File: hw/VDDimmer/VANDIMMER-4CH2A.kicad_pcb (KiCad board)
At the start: 4 copper layers, 100 x 84 mm, 98 parts, among them J1 USB-C 16P, J10 A2 V+SEL VIN/5V, J11 BTN1, J12 BTN2, J13 EXP 3V3/GND/SDA/SCL/EN/IO0, J14 UART1 3V3/GND/TX/RX, J2 VIN 12V, J3 CH1 LED-/V+, J4 CH2 LED-/V+, J5 CH3 LED-/V+, J6 CH4 LED-/V+, J7 ADDR1 V+/D/CLK/GND, J8 ADDR2 V+/D/CLK/GND, J9 A1 V+SEL VIN/5V, Q1 20N06, Q2 20N06, Q3 20N06, Q4 20N06, Q5 SUD50P06-15, U1 ESP32-S3-WROOM-1-N16R8, U2 AP63301WU-7, U3 BL1117-33CX, U4 74HCT125, U5 74HCT125

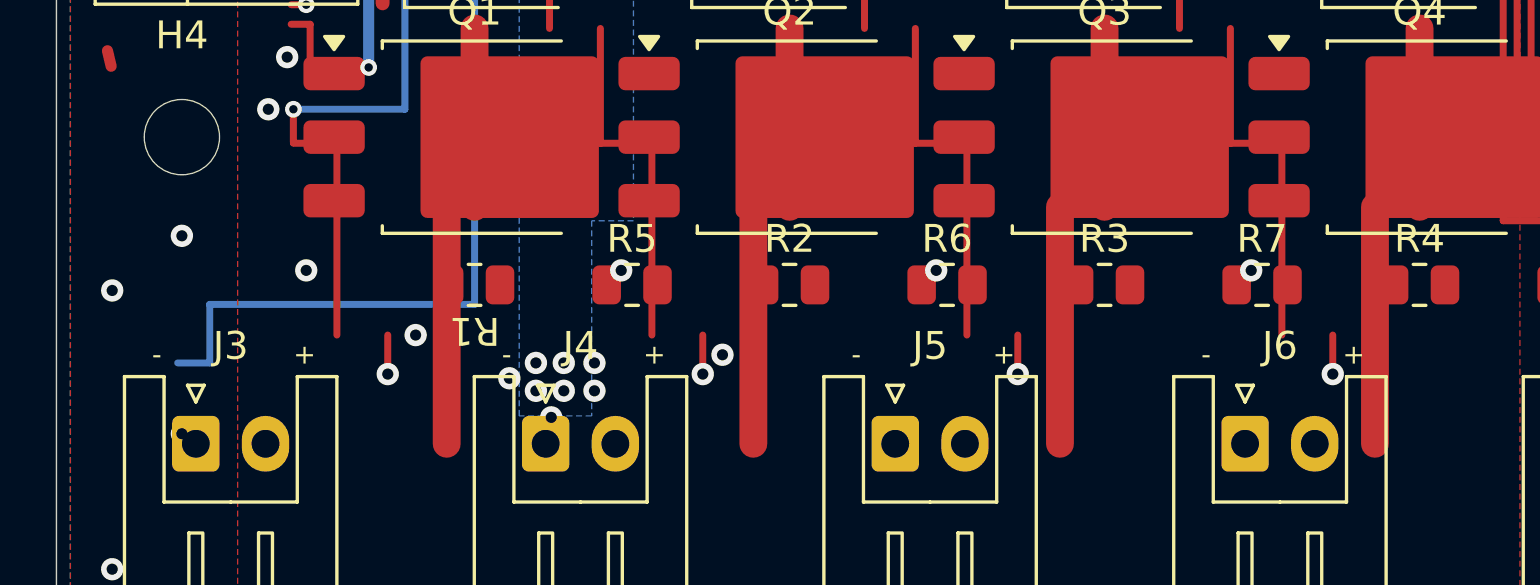
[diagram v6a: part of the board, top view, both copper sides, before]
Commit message: Mark J3-J6 terminals - and +, never GND
Eight F.SilkS marks at 0.8 mm, y 125.91, sitting in the band between the gate
resistors and the connector outlines - the only silk that stays readable once
a connector body is fitted, since the plug approaches from off the board edge.

Verified against NETS, not pin numbers: each - resolves to a DRAINn pad and
each + to VIN_PROT. That is the check that matters, because Rev A carries the
opposite polarity and grounding its pin 1 shorts the supply.

Spec section 6 is explicit that pin 1 must never be marked GND: it is a
switched MOSFET drain, open when the channel is off and floating to ~7 V on an
open terminal from flyback-diode and FET leakage alone.

R1 is rotated 180 -> 0. It was the only one of R1-R8 at 180, which rendered its
reference designator below the part instead of above and put it on top of J4's
- mark. Rotating it matches the rest of the row and clears the overlap; a
220R gate resistor is symmetric so rotation is cosmetic.

Gates: text_height violations 8 -> 0 (the earlier pass used 0.7 mm against the
project's 0.8 mm minimum); zero silk violations involving any polarity mark;
fpspace.py --courtyards still 0 overlaps.

Co-Authored-By: Claude Opus 5 (1M context) <noreply@anthropic.com>
Claude-Session: https://claude.ai/code/session_01YZHVU8aymL4RkLeCfwomwj
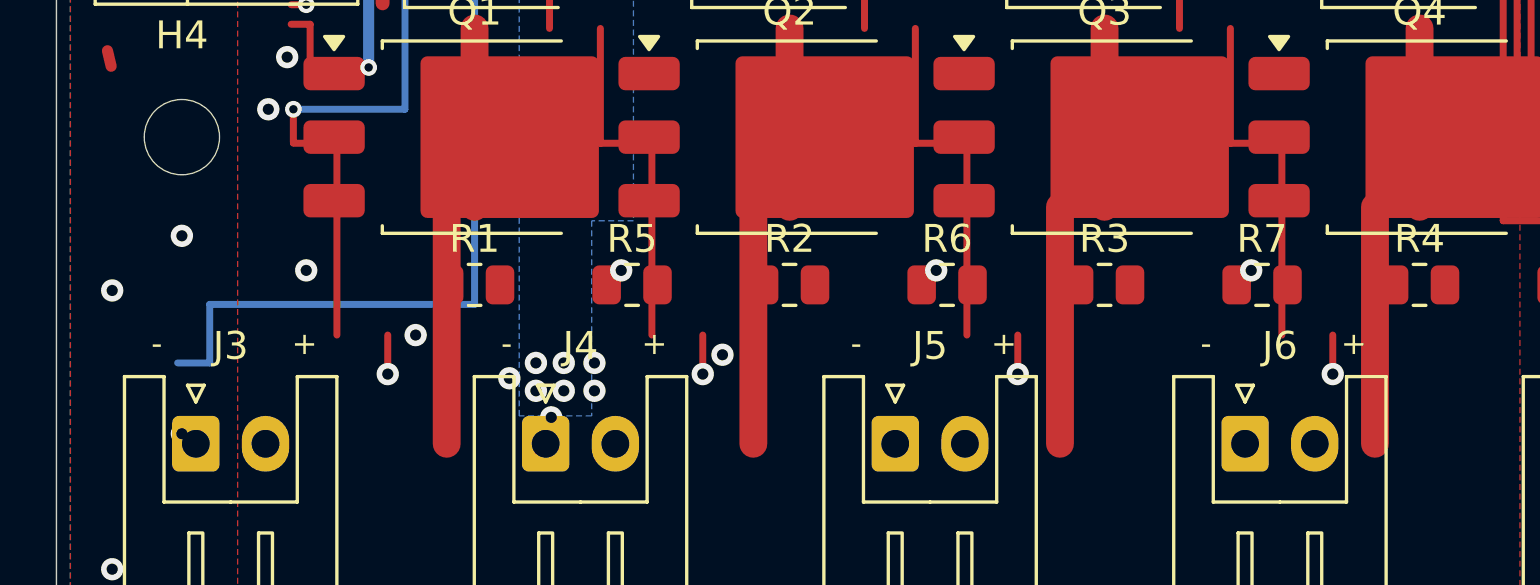
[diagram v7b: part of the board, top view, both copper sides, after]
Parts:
- turned R1 to 0 degrees
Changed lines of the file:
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@@
 	(footprint "Resistor_SMD:R_0805_2012Metric"
 		(layer "F.Cu")
-		(at 115 123.8 180)
+		(at 115 123.8)
 		(descr "Resistor SMD 0805 (2012 Metric), square (rectangular) end terminal, IPC-7351 nominal, (Body size source: IPC-SM-782 page 72, https://www.pcb-3d.com/wordpress/wp-content/uploads/ipc-sm-782a_amendment_1_and_2.pdf)")
 		(tags "resistor")
 		(property "Reference" "R1"
-			(at 0 -1.649999 180)
+			(at 0 -1.649999 0)
 			(unlocked yes)
 			(layer "F.SilkS")
@@
 		)
 		(property "Value" "220R"
-			(at 0 1.65 180)
+			(at 0 1.65 0)
 			(unlocked yes)
 			(layer "F.SilkS")
@@
 		)
 		(property "Datasheet" ""
-			(at 0 0 180)
+			(at 0 0 0)
 			(layer "F.Fab")
 			(hide yes)
@@
 		)
 		(property "Description" ""
-			(at 0 0 180)
+			(at 0 0 0)
 			(layer "F.Fab")
 			(hide yes)
@@
 		)
 		(property "KiLib_Generator" "SMD_2terminal_chip_molded"
-			(at 0 0 180)
+			(at 0 0 0)
 			(layer "F.SilkS")
 			(hide yes)
@@
 		)
 		(property "LCSC" "C17557"
-			(at 0 0 180)
+			(at 0 0 0)
 			(unlocked yes)
 			(layer "F.Fab")
@@
 		)
 		(property "MPN" "0805W8F2200T5E"
-			(at 0 0 180)
+			(at 0 0 0)
 			(unlocked yes)
 			(layer "F.Fab")
@@
 		)
 		(property "Manufacturer" "UNI-ROYAL"
-			(at 0 0 180)
+			(at 0 0 0)
 			(unlocked yes)
 			(layer "F.Fab")
@@
 		(duplicate_pad_numbers_are_jumpers no)
 		(fp_line
-			(start -0.227064 0.735)
-			(end 0.227064 0.735)
+			(start -0.227064 -0.735)
+			(end 0.227064 -0.735)
 			(stroke
 				(width 0.12)
@@
 		)
 		(fp_line
-			(start -0.227064 -0.735)
-			(end 0.227064 -0.735)
+			(start -0.227064 0.735)
+			(end 0.227064 0.735)
 			(stroke
 				(width 0.12)
@@
 		)
 		(fp_text user "${REFERENCE}"
-			(at 0 0 180)
+			(at 0 0 0)
 			(unlocked yes)
 			(layer "F.Fab")
@@
 		)
 		(pad "1" smd roundrect
-			(at -0.9125 0 180)
+			(at -0.9125 0)
 			(size 1.025 1.4)
 			(layers "F.Cu" "F.Mask" "F.Paste")
@@
 		)
 		(pad "2" smd roundrect
-			(at 0.9125 0 180)
+			(at 0.9125 0)
 			(size 1.025 1.4)
 			(layers "F.Cu" "F.Mask" "F.Paste")
@@
 	)
 	(gr_text "-"
-		(at 103.6 126.3 0)
+		(at 103.6 125.91 0)
 		(layer "F.SilkS")
 		(effects
 			(font
-				(size 0.7 0.7)
-				(thickness 0.105)
+				(size 0.8 0.8)
+				(thickness 0.12)
 			)
 		)
 	)
 	(gr_text "+"
-		(at 108.9 126.3 0)
+		(at 108.9 125.91 0)
 		(layer "F.SilkS")
 		(effects
 			(font
-				(size 0.7 0.7)
-				(thickness 0.105)
+				(size 0.8 0.8)
+				(thickness 0.12)
 			)
 		)
 	)
 	(gr_text "-"
-		(at 116.15 126.3 0)
+		(at 116.15 125.91 0)
 		(layer "F.SilkS")
 		(effects
 			(font
-				(size 0.7 0.7)
-				(thickness 0.105)
+				(size 0.8 0.8)
+				(thickness 0.12)
 			)
 		)
 	)
 	(gr_text "+"
-		(at 121.45 126.3 0)
+		(at 121.45 125.91 0)
 		(layer "F.SilkS")
 		(effects
 			(font
-				(size 0.7 0.7)
-				(thickness 0.105)
+				(size 0.8 0.8)
+				(thickness 0.12)
 			)
 		)
 	)
 	(gr_text "-"
-		(at 128.69 126.3 0)
+		(at 128.69 125.91 0)
 		(layer "F.SilkS")
 		(effects
 			(font
-				(size 0.7 0.7)
-				(thickness 0.105)
+				(size 0.8 0.8)
+				(thickness 0.12)
 			)
 		)
 	)
 	(gr_text "+"
-		(at 133.99 126.3 0)
+		(at 133.99 125.91 0)
 		(layer "F.SilkS")
 		(effects
 			(font
-				(size 0.7 0.7)
-				(thickness 0.105)
+				(size 0.8 0.8)
+				(thickness 0.12)
 			)
 		)
 	)
 	(gr_text "-"
-		(at 141.24 126.3 0)
+		(at 141.24 125.91 0)
 		(layer "F.SilkS")
 		(effects
 			(font
-				(size 0.7 0.7)
-				(thickness 0.105)
+				(size 0.8 0.8)
+				(thickness 0.12)
 			)
 		)
 	)
 	(gr_text "+"
-		(at 146.54 126.3 0)
+		(at 146.54 125.91 0)
 		(layer "F.SilkS")
 		(effects
 			(font
-				(size 0.7 0.7)
-				(thickness 0.105)
+				(size 0.8 0.8)
+				(thickness 0.12)
 			)
 		)

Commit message: Rev B placement complete, rendered for review
Three outputs in renders/: the plan's F.Cu view, a clean silk/fab/outline view
(stale Rev A copper obscures the placement otherwise), and the 3D top render.

Placement gates pass:
  fpspace.py --courtyards   0 overlaps, exit 0
  measure.py section 1      hot loop 2.51 mm2, 0 vias (gate < 15)
  Edge.Cuts containment     only U1 outside, antenna overhang by design

DRC's 1037 violations and 193 unconnected items are Rev A's copper still lying
where the old placement put it while every component has moved. That is the
expected pre-routing state, not a regression; Phase 5 rips it up. The gates
that mean anything before routing are the three above.

The render found two silkscreen defects that no numeric gate would have caught:

1. The board is silkscreened "Rev A" at (164.3, 99.8). Not a missing Rev B
   mark - an actively WRONG one, on a board whose J3-J6 polarity is reversed
   from the Rev A it claims to be. This is checklist item 1.1 upgraded from
   "add" to "correct", and it is the single most important silk fix before fab.

2. The title block "VANDIMMER-4CH+2A / v 1.0" at (103.9..123.1, 74.0..78.0)
   now sits on top of the relocated buck cluster.

Both are free board texts, and Konnect can neither edit nor delete board text,
so both need a GUI pass. Two replacement areas verified clear of all
courtyards and footprint silk: x 102.3..122.3 y 95.8..101.8 for the title, and
x 145..163 y 79..92 for a large central REV B.

Co-Authored-By: Claude Opus 5 (1M context) <noreply@anthropic.com>
Claude-Session: https://claude.ai/code/session_01YZHVU8aymL4RkLeCfwomwj
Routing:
- net unconnected-(U1-IO14-Pad22): vias 1 -> 0
- net VIN_PROT: vias 15 -> 14
- net GND: vias 130 -> 132
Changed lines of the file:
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@@
 		(tags "phoenix_contact connector MC_01x02_G_5.08mm")
 		(property "Reference" "J2"
-			(at 2.54 -3 -90)
+			(at 2.54 -3 270)
 			(unlocked yes)
 			(layer "F.SilkS")
@@
 		)
 		(property "Value" "VIN 12V"
-			(at 2.54 9.2 -90)
+			(at 2.54 9.2 270)
 			(unlocked yes)
 			(layer "F.SilkS")
@@
 		)
 		(property "Datasheet" ""
-			(at 0 0 -90)
+			(at 0 0 270)
 			(layer "F.Fab")
 			(hide yes)
@@
 		)
 		(property "Description" ""
-			(at 0 0 -90)
+			(at 0 0 270)
 			(layer "F.Fab")
 			(hide yes)
@@
 		)
 		(property "KiLib_Generator" "connector/PhoenixContact"
-			(at 0 0 -90)
+			(at 0 0 270)
 			(layer "F.SilkS")
 			(hide yes)
@@
 		)
 		(property "Assembly" "hand-fit. 12 V ONLY - D5 is an SMBJ18A (18 V standoff); 24 V destroys it. The old '9-24V' label predated the 12 V-only decision"
-			(at 0 0 -90)
+			(at 0 0 270)
 			(unlocked yes)
 			(layer "F.Fab")
@@
 		)
 		(property "MPN" "MC 1,5/2-G-5.08"
-			(at 0 0 -90)
+			(at 0 0 270)
 			(unlocked yes)
 			(layer "F.Fab")
@@
 		)
 		(property "Manufacturer" "Phoenix Contact"
-			(at 0 0 -90)
+			(at 0 0 270)
 			(unlocked yes)
 			(layer "F.Fab")
@@
 		)
 		(fp_text user "${REFERENCE}"
-			(at 2.54 -0.5 -90)
+			(at 2.54 -0.5 270)
 			(unlocked yes)
 			(layer "F.Fab")
@@
 		)
 		(pad "1" thru_hole roundrect
-			(at 0 0 -90)
+			(at 0 0 270)
 			(size 1.8 3.6)
 			(drill 1.2)
@@
 		)
 		(pad "2" thru_hole oval
-			(at 5.08 0 -90)
+			(at 5.08 0 270)
 			(size 1.8 3.6)
 			(drill 1.2)
@@
 		)
 		(property "Value" "ESP32-S3-WROOM-1-N16R8"
-			(at 0 14.6 -90)
+			(at 0 14.6 270)
 			(unlocked yes)
 			(layer "F.Fab")
@@
 		)
 		(property "Datasheet" ""
-			(at 0 0 -90)
+			(at 0 0 270)
 			(unlocked yes)
 			(layer "F.Fab")
@@
 		)
 		(property "Description" ""
-			(at 0 0 -90)
+			(at 0 0 270)
 			(unlocked yes)
 			(layer "F.Fab")
@@
 		)
 		(property "Assembly" "355 mA TX / 95 mA RX - this is the load U3 must carry"
-			(at 0 0 -90)
+			(at 0 0 270)
 			(unlocked yes)
 			(layer "F.Fab")
@@
 		)
 		(property "LCSC" "C2913202"
-			(at 0 0 -90)
+			(at 0 0 270)
 			(unlocked yes)
 			(layer "F.Fab")
@@
 		)
 		(property "MPN" "ESP32-S3-WROOM-1-N16R8"
-			(at 0 0 -90)
+			(at 0 0 270)
 			(unlocked yes)
 			(layer "F.Fab")
@@
 		)
 		(property "Manufacturer" "Espressif Systems"
-			(at 0 0 -90)
+			(at 0 0 270)
 			(unlocked yes)
 			(layer "F.Fab")
@@
 		)
 		(fp_text user "Antenna"
-			(at -0.05 -9.44 -90)
+			(at -0.05 -9.44 270)
 			(layer "Cmts.User")
 			(effects
@@
 		)
 		(fp_text user "KEEP-OUT ZONE"
-			(at 0 -18.92 -90)
+			(at 0 -18.92 270)
 			(layer "Cmts.User")
 			(effects
@@
 		)
 		(fp_text user "${REFERENCE}"
-			(at 0 -0.6 -90)
+			(at 0 -0.6 270)
 			(unlocked yes)
 			(layer "F.Fab")
@@
 		)
 		(pad "" smd rect
-			(at -2.9 1.06 -90)
+			(at -2.9 1.06 270)
 			(size 0.9 0.9)
 			(layers "F.Paste")
@@
 		)
 		(pad "" smd rect
-			(at -2.9 3.86 -90)
+			(at -2.9 3.86 270)
 			(size 0.9 0.9)
 			(layers "F.Paste")
@@
 		)
 		(pad "1" smd rect
-			(at -8.75 -5.26 -90)
+			(at -8.75 -5.26 270)
 			(size 1.5 0.9)
 			(layers "F.Cu" "F.Mask" "F.Paste")
@@
 		)
 		(pad "2" smd rect
-			(at -8.75 -3.99 -90)
+			(at -8.75 -3.99 270)
 			(size 1.5 0.9)
 			(layers "F.Cu" "F.Mask" "F.Paste")
@@
 		)
 		(pad "3" smd rect
-			(at -8.75 -2.72 -90)
+			(at -8.75 -2.72 270)
 			(size 1.5 0.9)
 			(layers "F.Cu" "F.Mask" "F.Paste")
@@
 		)
 		(pad "4" smd rect
-			(at -8.75 -1.45 -90)
+			(at -8.75 -1.45 270)
 			(size 1.5 0.9)
 			(layers "F.Cu" "F.Mask" "F.Paste")
@@
 		)
 		(pad "5" smd rect
-			(at -8.75 -0.18 -90)
+			(at -8.75 -0.18 270)
 			(size 1.5 0.9)
 			(layers "F.Cu" "F.Mask" "F.Paste")
@@
 		)
 		(pad "6" smd rect
-			(at -8.75 1.09 -90)
+			(at -8.75 1.09 270)
 			(size 1.5 0.9)
 			(layers "F.Cu" "F.Mask" "F.Paste")
@@
 		)
 		(pad "7" smd rect
-			(at -8.75 2.36 -90)
+			(at -8.75 2.36 270)
 			(size 1.5 0.9)
 			(layers "F.Cu" "F.Mask" "F.Paste")
@@
 		)
 		(pad "8" smd rect
-			(at -8.75 3.63 -90)
+			(at -8.75 3.63 270)
 			(size 1.5 0.9)
 			(layers "F.Cu" "F.Mask" "F.Paste")
@@
 		)
 		(pad "9" smd rect
-			(at -8.75 4.9 -90)
+			(at -8.75 4.9 270)
 			(size 1.5 0.9)
 			(layers "F.Cu" "F.Mask" "F.Paste")
@@
 		)
 		(pad "10" smd rect
-			(at -8.75 6.17 -90)
+			(at -8.75 6.17 270)
 			(size 1.5 0.9)
 			(layers "F.Cu" "F.Mask" "F.Paste")
@@
 		)
 		(pad "11" smd rect
-			(at -8.75 7.44 -90)
+			(at -8.75 7.44 270)
 			(size 1.5 0.9)
 			(layers "F.Cu" "F.Mask" "F.Paste")
@@
 		)
 		(pad "12" smd rect
-			(at -8.75 8.71 -90)
+			(at -8.75 8.71 270)
 			(size 1.5 0.9)
 			(layers "F.Cu" "F.Mask" "F.Paste")
@@
 		)
 		(pad "13" smd rect
-			(at -8.75 9.98 -90)
+			(at -8.75 9.98 270)
 			(size 1.5 0.9)
 			(layers "F.Cu" "F.Mask" "F.Paste")
@@
 		)
 		(pad "27" smd rect
-			(at 8.75 11.25 -90)
+			(at 8.75 11.25 270)
 			(size 1.5 0.9)
 			(layers "F.Cu" "F.Mask" "F.Paste")
@@
 		)
 		(pad "28" smd rect
-			(at 8.75 9.98 -90)
+			(at 8.75 9.98 270)
 			(size 1.5 0.9)
 			(layers "F.Cu" "F.Mask" "F.Paste")
@@
 		)
 		(pad "29" smd rect
-			(at 8.75 8.71 -90)
+			(at 8.75 8.71 270)
 			(size 1.5 0.9)
 			(layers "F.Cu" "F.Mask" "F.Paste")
@@
 		)
 		(pad "30" smd rect
-			(at 8.75 7.44 -90)
+			(at 8.75 7.44 270)
 			(size 1.5 0.9)
 			(layers "F.Cu" "F.Mask" "F.Paste")
@@
 		)
 		(pad "31" smd rect
-			(at 8.75 6.17 -90)
+			(at 8.75 6.17 270)
 			(size 1.5 0.9)
 			(layers "F.Cu" "F.Mask" "F.Paste")
@@
 		)
 		(pad "32" smd rect
-			(at 8.75 4.9 -90)
+			(at 8.75 4.9 270)
 			(size 1.5 0.9)
 			(layers "F.Cu" "F.Mask" "F.Paste")
@@
 		)
 		(pad "33" smd rect
-			(at 8.75 3.63 -90)
+			(at 8.75 3.63 270)
 			(size 1.5 0.9)
 			(layers "F.Cu" "F.Mask" "F.Paste")
@@
 		)
 		(pad "34" smd rect
-			(at 8.75 2.36 -90)
+			(at 8.75 2.36 270)
 			(size 1.5 0.9)
 			(layers "F.Cu" "F.Mask" "F.Paste")
@@
 		)
 		(pad "35" smd rect
-			(at 8.75 1.09 -90)
+			(at 8.75 1.09 270)
 			(size 1.5 0.9)
 			(layers "F.Cu" "F.Mask" "F.Paste")
@@
 		)
 		(pad "36" smd rect
-			(at 8.75 -0.18 -90)
+			(at 8.75 -0.18 270)
 			(size 1.5 0.9)
 			(layers "F.Cu" "F.Mask" "F.Paste")
@@
 		)
 		(pad "37" smd rect
-			(at 8.75 -1.45 -90)
+			(at 8.75 -1.45 270)
 			(size 1.5 0.9)
 			(layers "F.Cu" "F.Mask" "F.Paste")
@@
 		)
 		(pad "38" smd rect
-			(at 8.75 -2.72 -90)
+			(at 8.75 -2.72 270)
 			(size 1.5 0.9)
 			(layers "F.Cu" "F.Mask" "F.Paste")
@@
 		)
 		(pad "39" smd rect
-			(at 8.75 -3.99 -90)
+			(at 8.75 -3.99 270)
 			(size 1.5 0.9)
 			(layers "F.Cu" "F.Mask" "F.Paste")
@@
 		)
 		(pad "40" smd rect
-			(at 8.75 -5.26 -90)
+			(at 8.75 -5.26 270)
 			(size 1.5 0.9)
 			(layers "F.Cu" "F.Mask" "F.Paste")
@@
 		)
 		(pad "41" thru_hole circle
-			(at -2.9 3.16 -90)
+			(at -2.9 3.16 270)
 			(size 0.6 0.6)
 			(drill 0.2)
@@
 		)
 		(pad "41" thru_hole circle
-			(at -2.2 1.06 -90)
+			(at -2.2 1.06 270)
 			(size 0.6 0.6)
 			(drill 0.2)
@@
 		)
 		(pad "41" thru_hole circle
-			(at -2.2 2.46 -90)
+			(at -2.2 2.46 270)
 			(size 0.6 0.6)
 			(drill 0.2)
@@
 		)
 		(pad "41" thru_hole circle
-			(at -2.2 3.86 -90)
+			(at -2.2 3.86 270)
 			(size 0.6 0.6)
 			(drill 0.2)
@@
 		)
 		(pad "41" thru_hole circle
-			(at -1.5 1.76 -90)
+			(at -1.5 1.76 270)
 			(size 0.6 0.6)
 			(drill 0.2)
@@
 		)
 		(pad "41" thru_hole circle
-			(at -1.5 3.16 -90)
+			(at -1.5 3.16 270)
 			(size 0.6 0.6)
 			(drill 0.2)
@@
 		)
 		(pad "41" thru_hole circle
-			(at -0.8 1.06 -90)
+			(at -0.8 1.06 270)
 			(size 0.6 0.6)
 			(drill 0.2)
@@
 		)
 		(pad "41" thru_hole circle
-			(at -0.8 2.46 -90)
+			(at -0.8 2.46 270)
 			(size 0.6 0.6)
 			(drill 0.2)
@@
 		)
 		(pad "41" thru_hole circle
-			(at -0.8 3.86 -90)
+			(at -0.8 3.86 270)
 			(size 0.6 0.6)
 			(drill 0.2)
@@
 		)
 		(pad "41" thru_hole circle
-			(at -0.1 1.76 -90)
+			(at -0.1 1.76 270)
 			(size 0.6 0.6)
 			(drill 0.2)
@@
 		)
 		(pad "41" thru_hole circle
-			(at -0.1 3.16 -90)
+			(at -0.1 3.16 270)
 			(size 0.6 0.6)
 			(drill 0.2)
@@
 	)
 	(via
-		(at 188.45 113.65)
-		(size 0.8)
-		(drill 0.4)
-		(layers "F.Cu" "B.Cu")
-		(net "VIN_PROT")
-	)
-	(via
 		(at 119.15 92.453)
 		(size 0.8)
@@
 	)
 	(via
+		(at 188.45 113.65)
+		(size 0.8)
+		(drill 0.4)
+		(layers "F.Cu" "B.Cu")
+		(net "GND")
+	)
+	(via
 		(at 126.234 106.966)
 		(size 0.8)
@@
 	)
 	(via
+		(at 126.721 101.436)
+		(size 0.8)
+		(drill 0.4)
+		(layers "F.Cu" "B.Cu")
+		(net "GND")
+	)
+	(via
 		(at 132 62)
 		(size 0.8)
@@
 		(net "unconnected-(U1-IO4-Pad4)")
 	)
-	(via
-		(at 126.721 101.436)
-		(size 0.8)
-		(drill 0.4)
-		(layers "F.Cu" "B.Cu")
-		(net "unconnected-(U1-IO14-Pad22)")
-	)
 	(zone
